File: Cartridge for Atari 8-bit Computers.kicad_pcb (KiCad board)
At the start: 2 copper layers, 55.1 x 55.6 mm, 15 parts, among them J1 Atari 8-bit Left Cartridge Co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, U0 27C128, U1 27C64, U2 74AHCT1G08

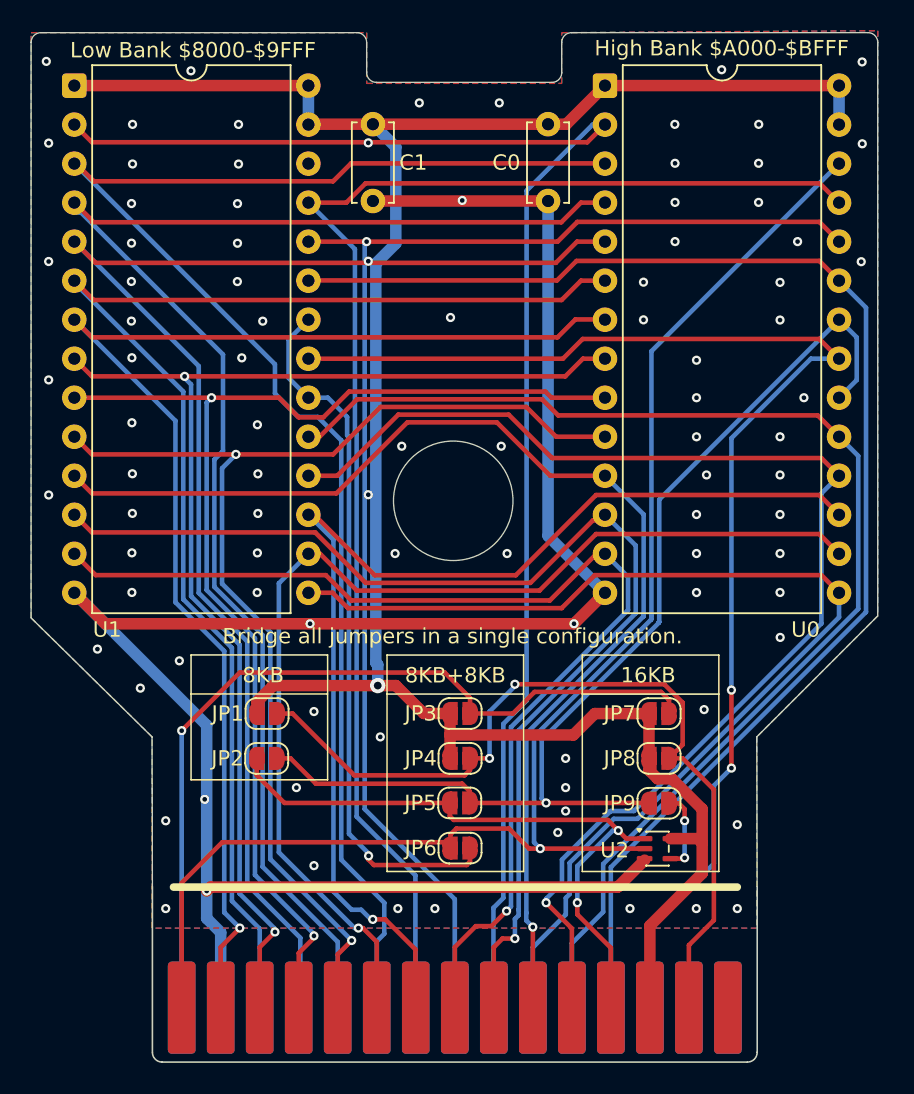
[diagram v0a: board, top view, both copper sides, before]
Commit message: Rename the project.
`Atari` being at the beginning of the name makes it seem like it's an
official project. Renaming should prevent any confusion.
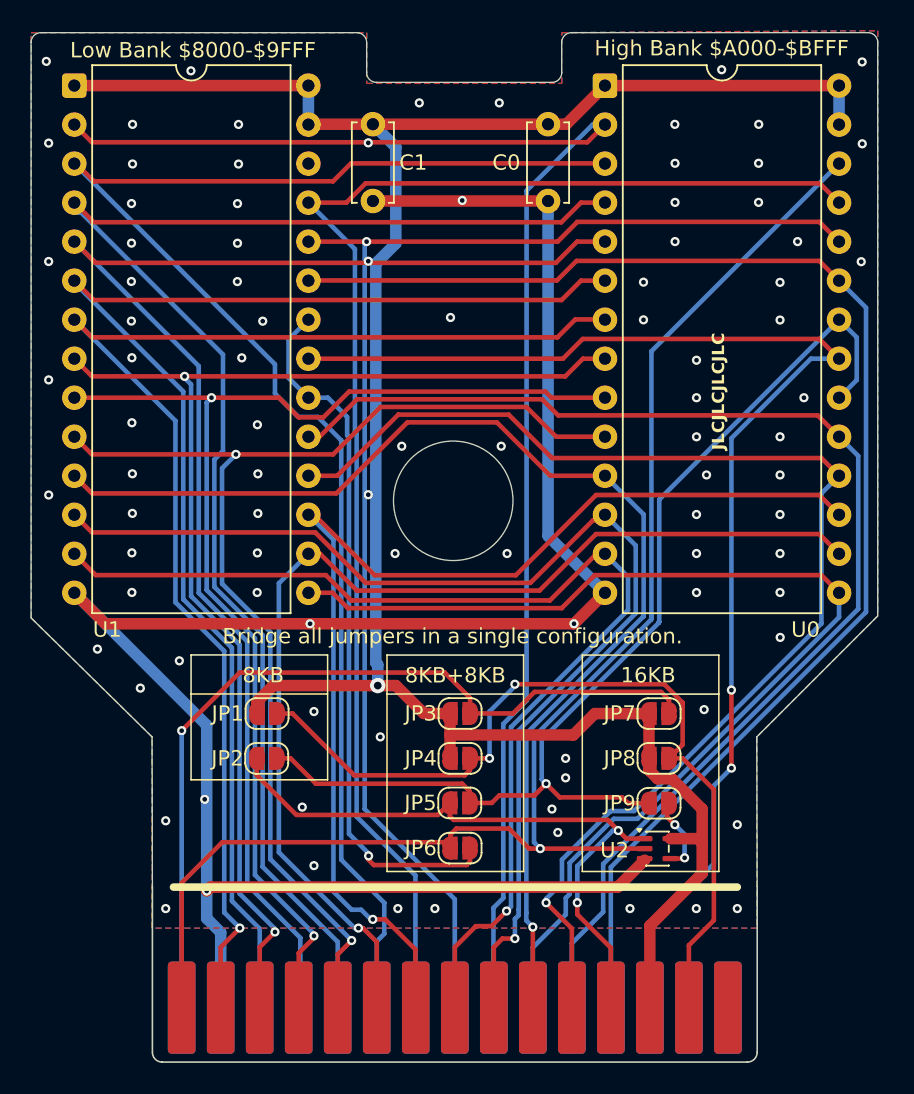
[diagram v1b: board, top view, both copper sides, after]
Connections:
- C0 pad 2: GND -> /U0_Enable_16KB
- C1 pad 2: GND -> /U0_Enable_16KB
- J1 pad B: GND -> /U0_Enable_16KB
- U0 pad 14: GND -> /U0_Enable_16KB
- U1 pad 14: GND -> /U0_Enable_16KB
- U2 pad 3: GND -> /U0_Enable_16KB
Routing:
- net GND: track 135.0 -> 0.00 mm, vias 95 -> 94
- net /U0_Enable_16KB: track 5.30 -> 140.0 mm, vias 2 -> 3
- net //S5: track 42.3 -> 43.0 mm
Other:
- board text added: "${PROJECTNAME_FULL} ${VERSION} ${CURRENT_DATE} ${COMPANY} ${PROJECTURL}"
- board text added: "JLCJLCJLCJLC"
- board text removed: "Atari 8-Bit (400/800/XL/XE) Cartridge V1.0 Sean D. Cline https://sdcline.com/atari8bitcart"

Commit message: Build the JLCPCB gerbers as a Github action.
Additionally, fix some DRC errors introduced with the stitching vias and
add a copyright disclaimer to the readme.
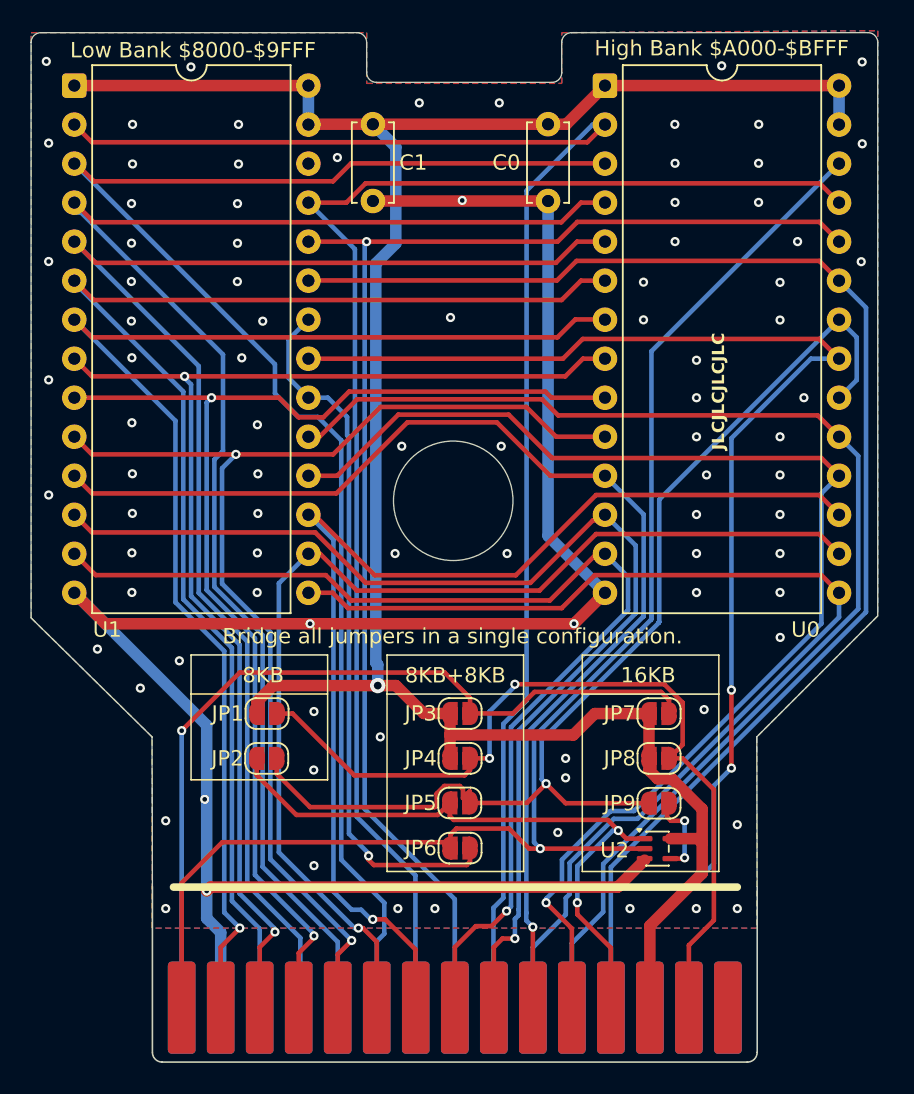
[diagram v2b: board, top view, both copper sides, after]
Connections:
- C0 pad 2: /U0_Enable_16KB -> GND
- C1 pad 2: /U0_Enable_16KB -> GND
- J1 pad B: /U0_Enable_16KB -> GND
- U0 pad 14: /U0_Enable_16KB -> GND
- U1 pad 14: /U0_Enable_16KB -> GND
- U2 pad 3: /U0_Enable_16KB -> GND
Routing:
- net GND: track 0.00 -> 135.0 mm, vias 94 -> 92
- net /U0_Enable_16KB: track 140.0 -> 5.55 mm, vias 3 -> 2
- net /U0_Enable: track 71.9 -> 74.7 mm

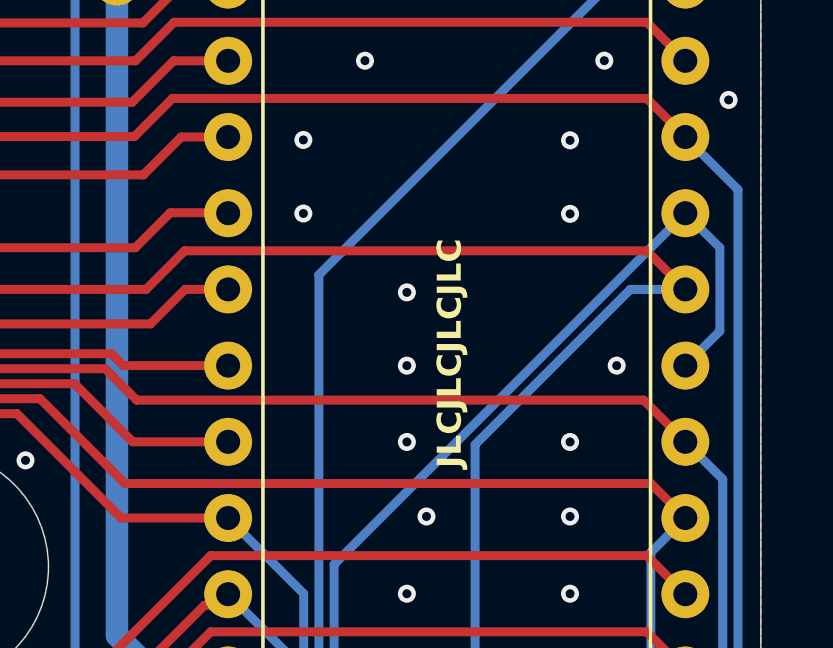
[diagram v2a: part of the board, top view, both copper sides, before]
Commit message: Remove JLCJLCJLCJLC placeholder text for run number.
It seems JLCPCB no longer needs a production run number anymore.

Additionally, generate preview images as during the CI build.
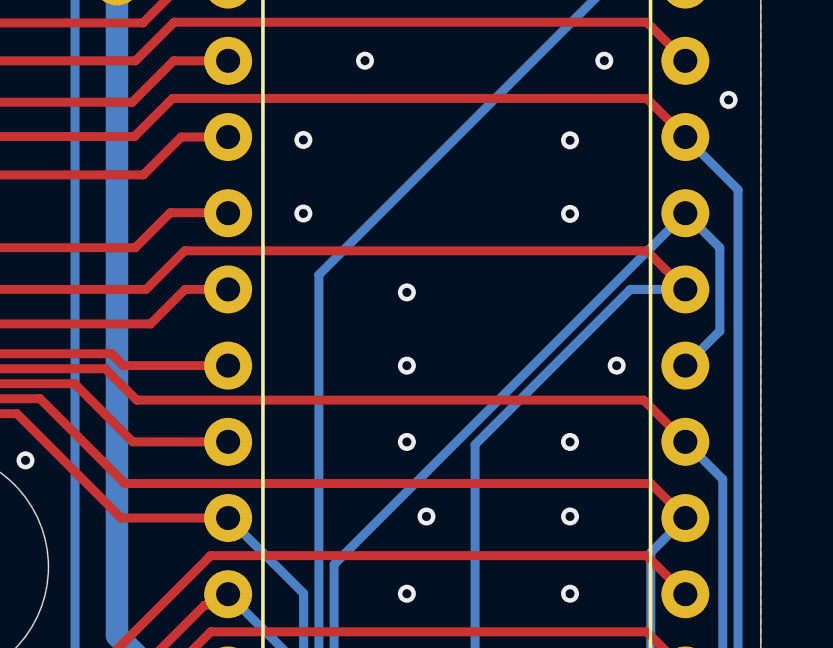
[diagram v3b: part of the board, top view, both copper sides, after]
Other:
- board text removed: "JLCJLCJLCJLC"
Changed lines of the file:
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@@
 		(layer "Edge.Cuts")
-	)
-	(gr_text "JLCJLCJLCJLC"
-		(at 124.968 84.201 90)
-		(layer "F.SilkS")
-		(effects
-			(font
-				(size 0.8 0.8)
-				(thickness 0.15)
-				(bold yes)
-			)
-			(justify left bottom)
-		)
 	)
 	(gr_text "Low Bank $8000-$9FFF"
